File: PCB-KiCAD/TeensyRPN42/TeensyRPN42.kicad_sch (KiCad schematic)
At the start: 47 parts, among them SW1 SW_DPST_x2, SW10 SW_DPST_x2, SW11 SW_DPST_x2, SW12 SW_DPST_x2, SW13 SW_DPST_x2, SW14 SW_DPST_x2, SW15 SW_DPST_x2, SW16 SW_DPST_x2, SW17 SW_DPST_x2, SW18 SW_DPST_x2, SW19 SW_DPST_x2, SW2 SW_DPST_x2, SW20 SW_DPST_x2, SW21 SW_DPST_x2, SW22 SW_DPST_x2, SW23 SW_DPST_x2, SW24 SW_DPST_x2, SW25 SW_DPST_x2, SW26 SW_DPST_x2, SW27 SW_DPST_x2, SW28 SW_DPST_x2, SW29 SW_DPST_x2, SW3 SW_DPST_x2, SW30 SW_DPST_x2, SW31 SW_DPST_x2, SW32 SW_DPST_x2, SW33 SW_DPST_x2, SW34 SW_DPST_x2, SW35 SW_DPST_x2, SW36 SW_DPST_x2, SW37 SW_DPST_x2, SW4 SW_DPST_x2, SW5 SW_DPST_x2, SW6 SW_DPST_x2, SW7 SW_DPST_x2, SW8 SW_DPST_x2, SW9 SW_DPST_x2, U1 74HC165, U2 74HC165, U3 74HC165, U4 74HC165, U5 74HC165

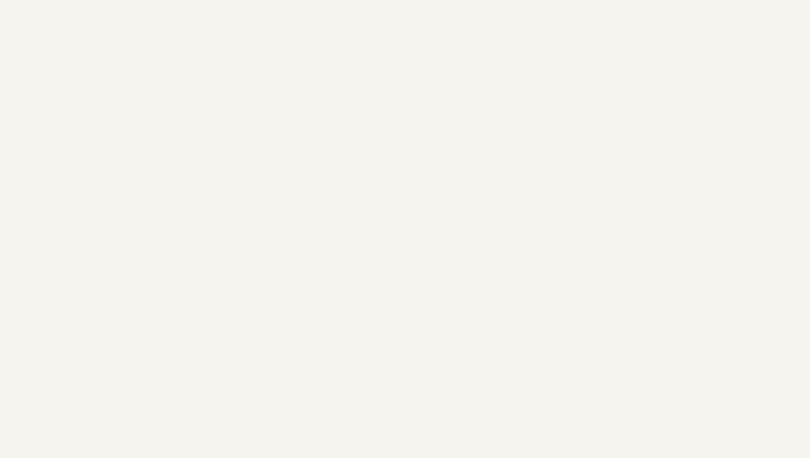
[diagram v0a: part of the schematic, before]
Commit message: Added KeyChoc stuff
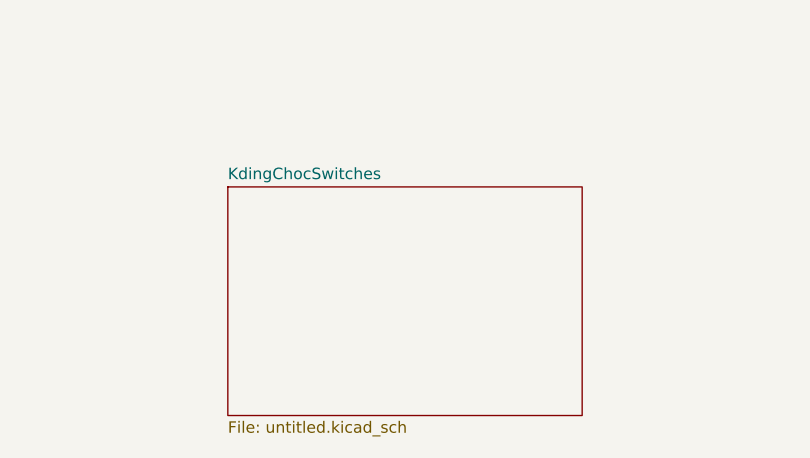
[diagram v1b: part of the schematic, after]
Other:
- added sheet KdingChocSwitches (untitled.kicad_sch)

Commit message: A little PCBing
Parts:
- removed RN1, RN2, RN3, RN4, RN5: R_Network08, Resistor_THT:R_Array_SIP9, symbol Device:R_Network08
- removed SW1, SW10, SW11, SW12, SW13, SW14, SW15, SW16, SW17, SW18, SW19, SW2, SW20, SW21, SW22, SW23, SW24, SW25, SW26, SW27, SW28, SW29, SW3, SW30, SW31, SW32, SW33, SW34, SW35, SW36, SW37, SW4, SW5, SW6, SW7, SW8, SW9: SW_DPST_x2, Button_Switch_THT:SW_PUSH-12mm, symbol Switch:SW_DPST_x2
- removed U1, U2, U3, U4, U5: 74HC165, Package_SO:SOIC-16W_5.3x10.2mm_P1.27mm, symbol 74xx:74HC165
- added DS1: OLED-128O064D, Display:OLED-128O064D, symbol Display_Graphic:OLED-128O064D
- added U2: STM32F411RETx, Package_QFP:LQFP-64_10x10mm_P0.5mm, symbol MCU_ST_STM32F4:STM32F411RETx
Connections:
- new net: U2.18 (VSS), U2.31 (VSS), U2.47 (VSS), U2.63 (VSS)
- new net: DS1.1 (GND), DS1.30 (GND)
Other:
- added sheet LEDS (leds.kicad_sch)

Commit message: more PCB
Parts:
- removed DS1: OLED-128O064D, Display:OLED-128O064D, symbol Display_Graphic:OLED-128O064D
- added C1, C2: 20pF, Capacitor_SMD:C_0603_1608Metric_Pad1.08x0.95mm_HandSolder, symbol Device:C
- added C10, C11, C12, C13, C3, C6, C7, C8, C9: 100nF, Capacitor_SMD:C_0603_1608Metric_Pad1.08x0.95mm_HandSolder, symbol Device:C
- added C4, C5: 10u, Capacitor_SMD:C_1206_3216Metric_Pad1.33x1.80mm_HandSolder, symbol Device:C_Polarized
- added H1, H2, H3, H4: MountingHole, MountingHole:MountingHole_3.2mm_M3_ISO7380, symbol Mechanical:MountingHole
- added J1: Conn_01x06, Connector_PinHeader_2.54mm:PinHeader_1x06_P2.54mm_Vertical, symbol Connector_Generic:Conn_01x06
- added J2: Conn_01x04, Connector_PinSocket_2.54mm:PinSocket_1x04_P2.54mm_Vertical, symbol Connector_Generic:Conn_01x04
- added J3: Conn_02x08_Odd_Even, RPN42Library:OLED-2.8inch16pin, symbol Connector_Generic:Conn_02x08_Odd_Even
- added JP1, JP2: Jumper_2_Small_Bridged, symbol Jumper:Jumper_2_Small_Bridged
- added L1, L2: L_Ferrite_Small, Inductor_SMD:L_0603_1608Metric_Pad1.05x0.95mm_HandSolder, symbol Device:L_Ferrite_Small
- added R1, R5: 10k, Resistor_SMD:R_0603_1608Metric_Pad0.98x0.95mm_HandSolder, symbol Device:R
- added R3, R4: 2.2k, Resistor_SMD:R_0603_1608Metric_Pad0.98x0.95mm_HandSolder, symbol Device:R
- added SW1, SW2: SW_Push_Dual, Button_Switch_SMD:SW_SPST_EVQQ2, symbol Switch:SW_Push_Dual
- added U1: AMS1117-3.3, Package_TO_SOT_SMD:SOT-223-3_TabPin2, symbol Regulator_Linear:AMS1117-3.3
- added Y1: Crystal 8MHz, Crystal:Crystal_SMD_HC49-SD_HandSoldering, symbol Device:Crystal
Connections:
- net GND: now reaches U2.12 (VSSA)
- net GND: now also U2.18 (VSS), U2.31 (VSS), U2.47 (VSS), U2.63 (VSS), C1.2, C10.2, C11.2, C12.2, C13.2, C2.2, C3.2, C4.2, C5.2, C7.2, C8.2, C9.2, J2.1 (Pin_1), J3.1 (Pin_1), J3.11 (Pin_11), J3.12 (Pin_12), R1.2, SW1.1, SW1.3, U1.1 (GND)
- net at U2.13 (VDDA): now also C6.1, C6.2, L1.2
- net USAR_TX: now reaches U2.16 (PA2)
- net USART_RX: now reaches U2.17 (PA3)
- net +3.3V: now reaches U2.19 (VDD)
- net +3.3V: now also U2.32 (VDD), U2.48 (VDD), U2.64 (VDD), C10.1, C11.1, C12.1, C5.1, C7.1, C8.1, C9.1, L1.1, L2.2, R3.1, R4.1, R5.1, U1.2 (VO)
- net OLED_CS: now reaches U2.20 (PA4)
- net OLED_CS: now also J3.16 (Pin_16)
- net SCK1: now reaches U2.21 (PA5)
- net SCK1: now also J3.4 (Pin_4)
- net MISO1: now reaches U2.22 (PA6)
- net MOSI1: now reaches U2.23 (PA7)
- net MOSI1: now also J3.5 (Pin_5)
- net LEDs: now reaches U2.29 (PB10)
- net COL0: now reaches U2.38 (PC7)
- net COL1: now reaches U2.39 (PC8)
- net COL2: now reaches U2.40 (PC9)
- net ROW0: now reaches U2.41 (PA8)
- net ROW1: now reaches U2.42 (PA9)
- net ROW2: now reaches U2.43 (PA10)
- net ROW3: now reaches U2.44 (PA11)
- net ROW4: now reaches U2.45 (PA12)
- net ROW5: now reaches U2.46 (PA13)
- net ROW5: now also JP1.1 (A)
- net ROW6: now reaches U2.49 (PA14)
- net ROW6: now also JP2.1 (A)
- net at U2.5 (PH0): now also C1.1, Y1.2
- net ROW7: now reaches U2.50 (PA15)
- net COL3: now reaches U2.51 (PC10)
- net COL4: now reaches U2.52 (PC11)
- net COL5: now reaches U2.53 (PC12)
- net SWO: now reaches U2.55 (PB3)
- net at U2.6 (PH1): now also C2.1, Y1.1
- net at U2.60 (BOOT0): now also R1.1, SW2.2, SW2.4
- net SCL1: now reaches U2.61 (PB8)
- net SCL1: now also J2.3 (Pin_3), R3.2
- net SDA1: now reaches U2.62 (PB9)
- net SDA1: now also J2.4 (Pin_4), R4.2
- net NRST: now reaches U2.7 (NRST)
- net NRST: now also C3.1, J3.15 (Pin_15), R5.2, SW1.2, SW1.4
- new net: SW2.1, SW2.3
- new net OLED_D/C: J3.14 (Pin_14)
- new net TCK: JP2.2 (B)
- new net TMS: JP1.2 (B)
- new net V-OLED: C13.1, J2.2 (Pin_2), J3.2 (Pin_2), L2.1
- new net VIN: C4.1, U1.3 (VI)
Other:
- note added: "2.8" OLED SPI <> 97mm x 32.5"
- note added: "BOOT0"
- note added: "Mini OLED"
- note added: "RESET"
- note added: "STLink ! OLED mini or full ? An aus Schalterle? Lipo Kram ? WS8212 driver 5V IR IO ?"

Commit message: more pcb ...
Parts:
- removed JP1, JP2: Jumper_2_Small_Bridged, symbol Jumper:Jumper_2_Small_Bridged
- removed U1: AMS1117-3.3, Package_TO_SOT_SMD:SOT-223-3_TabPin2, symbol Regulator_Linear:AMS1117-3.3
- removed U2: STM32F411RETx, Package_QFP:LQFP-64_10x10mm_P0.5mm, symbol MCU_ST_STM32F4:STM32F411RETx
- added C26: 1nF, Capacitor_SMD:C_0603_1608Metric_Pad1.08x0.95mm_HandSolder, symbol Device:C
- added J4: Serial, Connector_PinHeader_2.54mm:PinHeader_1x03_P2.54mm_Vertical, symbol Connector_Generic:Conn_01x03
- added J5: Bat JST, Connector_JST:JST_EH_S2B-EH_1x02_P2.50mm_Horizontal, symbol Connector_Generic:Conn_01x02
- added Q2: IRLML6401, Package_TO_SOT_SMD:SOT-23, symbol Transistor_FET:IRLML6401
- added U2: STM32F405RGTx, Package_QFP:LQFP-64_10x10mm_P0.5mm, symbol MCU_ST_STM32F4:STM32F405RGTx
- added U4: MCP1727-3302xSN, Package_SO:SOIC-8_3.9x4.9mm_P1.27mm, symbol Regulator_Linear:MCP1727-3302xSN
- added Y3: Crystal_GND24, Crystal:Crystal_SMD_0603-4Pin_6.0x3.5mm_HandSoldering, symbol Device:Crystal_GND24
- J1: value Conn_01x06 -> SWD
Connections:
- net +3.3V: now also U2.19 (VDD), U2.32 (VDD), U2.48 (VDD), U2.64 (VDD), U4.7 (Sense), U4.8 (Vout)
- net COL0: now also U2.38 (PC7)
- net COL1: now also U2.39 (PC8)
- net COL2: now also U2.40 (PC9)
- net COL3: now also U2.51 (PC10)
- net COL4: now also U2.52 (PC11)
- net COL5: now also U2.53 (PC12)
- net GND: now also C6.2, J1.3 (Pin_3), SW2.1, SW2.3, C26.2, J4.1 (Pin_1), J5.1 (Pin_1), U2.18 (VSS), U2.63 (VSS), U4.4 (GND), Y3.2 (G), Y3.4 (G)
- net LEDs: now also U2.29 (PB10)
- net MISO1: now also U2.22 (PA6)
- net MOSI1: now also U2.23 (PA7)
- net NRST: now also J1.5 (Pin_5), U2.7 (NRST), U4.5 (PWRGD)
- net OLED_CS: now also U2.20 (PA4)
- net ROW0: now also U2.41 (PA8)
- net ROW1: now also U2.42 (PA9)
- net ROW2: now also U2.43 (PA10)
- net ROW7: now also U2.50 (PA15)
- net SCK1: now also U2.21 (PA5)
- net SCL1: now also U2.61 (PB8)
- net SDA1: now also U2.62 (PB9)
- net SWO: now also J1.6 (Pin_6), U2.55 (PB3)
- net TCK: now also J1.2 (Pin_2), U2.49 (PA14)
- net TMS: now also J1.4 (Pin_4), U2.46 (PA13)
- net USART_RX: now also J4.3 (Pin_3), U2.17 (PA3)
- net USAR_TX: now also J4.2 (Pin_2), U2.16 (PA2)
- net VIN: now also U4.1 (Vin), U4.2 (Vin)
- net VDDA: now reaches C6.1, L1.2
- net VDDA: now also U2.13 (VDDA); no longer C6.2
- net at C1.1, Y1.2: now also U2.5 (PH0), Y3.3
- net at C2.1, Y1.1: now also U2.6 (PH1), Y3.1
- net at R1.1, SW2.2, SW2.4: now also U2.60 (BOOT0)
- new net: C26.1, U4.6 (Cdelay)
- new net USB-D+: U2.45 (PA12)
- new net USB-D-: U2.44 (PA11)
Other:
- added sheet Stuff (stuff.kicad_sch)
- note added: "LowDrop 0.35V -> MCP1727"
- note added: "SWD+Ser ? Enter weg, 2 Tasten rein Oder reinschieben und 2 mini Schalter rein Dioden in Key Matrix ?"
- moved on the sheet: C10, C11, C12, C4, C5, C6, C7, C8, C9, J1, L1, Y1

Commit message: kram
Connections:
- net SWO: no longer U2.55 (PB3)
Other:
- note added: "PlatformIO stlink ok without SWO"
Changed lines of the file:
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@@
+		)
+	)
+	(text "PlatformIO stlink ok without SWO"
+		(exclude_from_sim no)
+		(at 46.736 148.336 0)
+		(effects
+			(font
+				(size 1.27 1.27)
+			)
 		)
 	)
@@
 	(wire
 		(pts
-			(xy 135.89 96.52) (xy 153.67 96.52)
-		)
-		(stroke
-			(width 0)
-			(type default)
-		)
-	)
-	(wire
-		(pts
 			(xy 57.15 53.34) (xy 76.2 53.34)
 		)
@@
 		(effects
 			(font
-				(size 1.27 1.27)
-			)
-			(justify left bottom)
-		)
-	)
-	(label "SWO"
-		(at 144.78 96.52 0)
-		(effects
-			(font
